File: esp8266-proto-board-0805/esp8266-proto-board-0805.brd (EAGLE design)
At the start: 29.1 x 32.7 mm, 13 parts

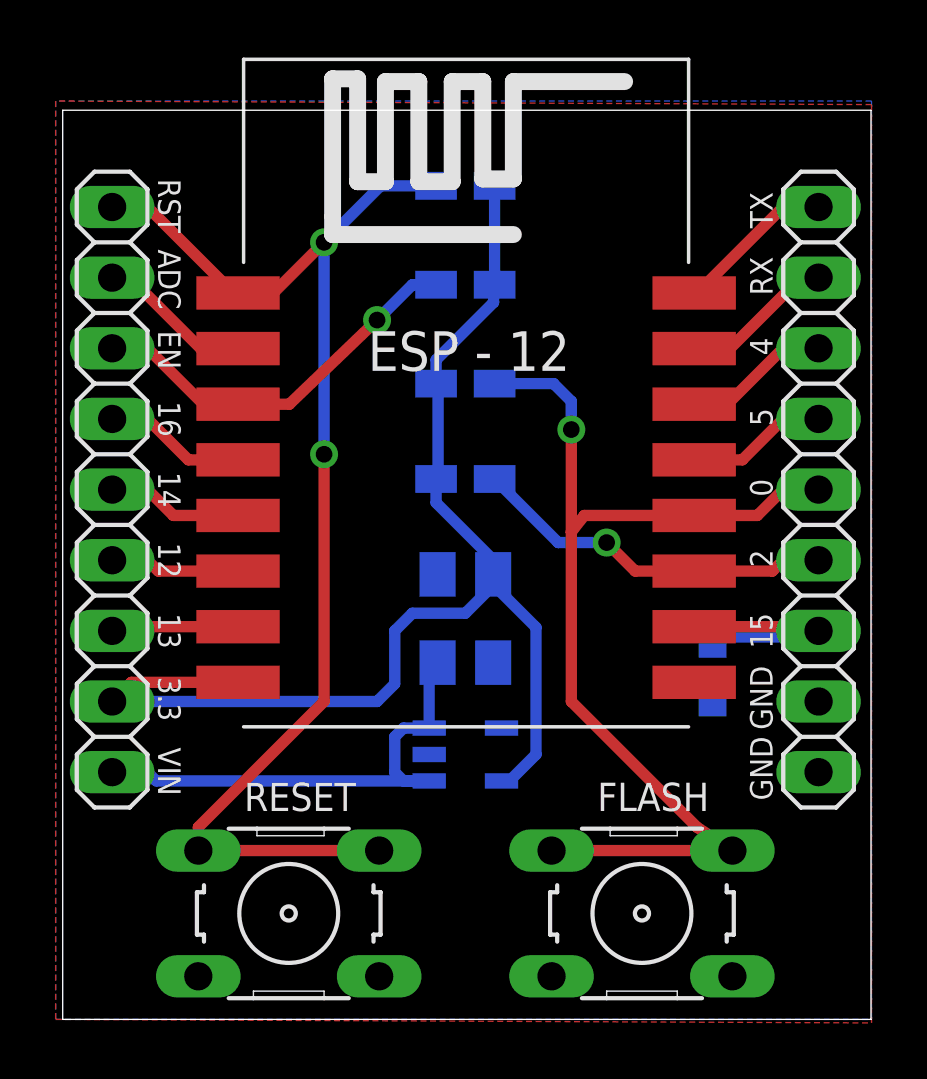
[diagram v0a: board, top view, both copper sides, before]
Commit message: reworked 0805 version with better footprint
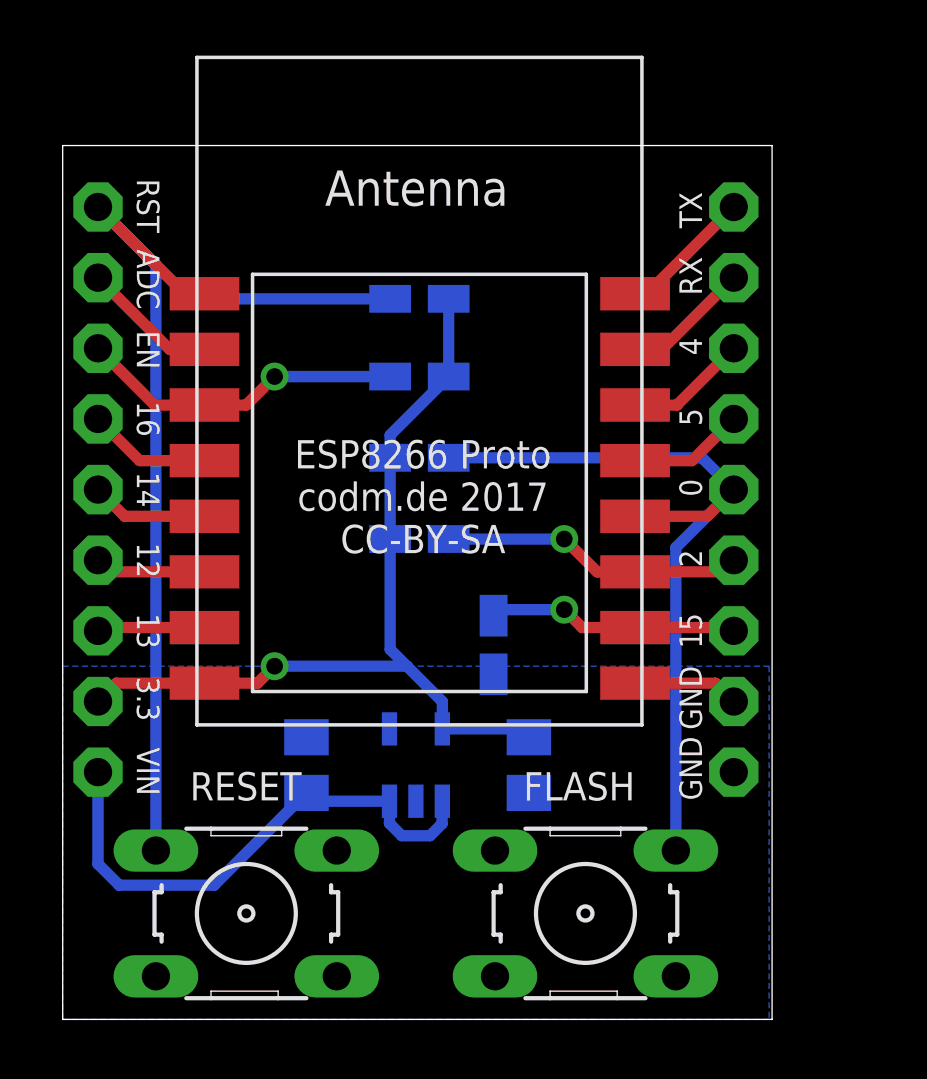
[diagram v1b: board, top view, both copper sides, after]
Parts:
- JP1, JP2: device pinhead:1X09 -> adafruit:1X09-BIG
- U1: device esp8266modules:ESP12-SMD -> adafruit:ESP-12
- moved R5 7.91 mm to (15.5, 13.5)
- moved C2 7.23 mm to (16.8, 9.14), turned to 90 degrees
- moved C1 6.80 mm to (8.76, 9.14), turned to 270 degrees
- moved R1 4.39 mm to (12.8, 25.9)
- moved R2 3.69 mm to (12.8, 23.1)
- moved R3 3.14 mm to (12.8, 20.2)
- moved JP1 3.05 mm to (24.1, 19.1)
- moved R4 2.72 mm to (12.8, 17.3)
- moved U1 2.18 mm to (12.8, 21.6)
- moved S1 2.03 mm to (18.8, 3.81), turned to 0 degrees
- moved VR 1.82 mm to (12.7, 9.14), turned to 0 degrees
- moved S2 1.52 mm to (6.60, 3.81), turned to 0 degrees
- moved JP2 0.51 mm to (1.27, 19.1)
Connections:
- net +3V3: now also U1.8; no longer U1.VCC
- net ADC: now also U1.2; no longer U1.ADC
- net CH_PD: now also U1.3; no longer U1.CH_PD
- net GND: now also S1.4, S2.3, U1.9; no longer S1.1, S1.2, S2.1, S2.2, U1.GND
- net GPIO0: now also S1.2, U1.12; no longer S1.3, S1.4, U1.GPIO0
- net GPIO12: now also U1.6; no longer U1.GPIO12
- net GPIO13: now also U1.7; no longer U1.GPIO13
- net GPIO14: now also U1.5; no longer U1.GPIO14
- net GPIO15: now also U1.10; no longer U1.GPIO15
- net GPIO16: now also U1.4; no longer U1.GPIO16
- net GPIO2: now also U1.11; no longer U1.GPIO2
- net GPIO4: now also U1.14; no longer U1.GPIO4
- net GPIO5: now also U1.13; no longer U1.GPIO5
- net RST: now also S2.1, U1.1; no longer S2.3, S2.4, U1.RESET
- net RX: now also U1.15; no longer U1.RXD0
- net TX: now also U1.16; no longer U1.TXD0
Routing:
- net +3V3: track 47.4 -> 32.0 mm, vias 0 -> 1
- net GPIO0: track 37.8 -> 28.5 mm, vias 1 -> 0
- net GND: track 0.00 -> 3.82 mm
- net CH_PD: track 14.8 -> 11.8 mm
- net GPIO2: track 13.2 -> 10.9 mm
- net RST: track 44.9 -> 43.9 mm, vias 2 -> 0
- net VIN: track 18.5 -> 19.5 mm
- net TX: track 5.75 -> 4.84 mm
- net RX: track 5.53 -> 4.62 mm
- net GPIO5: track 5.08 -> 4.17 mm
- net GPIO4: track 5.31 -> 4.39 mm
- net GPIO13: track 4.59 -> 3.88 mm
- net GPIO16: track 5.14 -> 4.45 mm
- net ADC: track 5.58 -> 4.90 mm
- net GPIO14: track 4.91 -> 4.23 mm
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- removed copper zone on layer 1, net GND
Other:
- board size 29.1 x 32.7 mm -> 25.5 x 31.4 mm
- board text added: "ESP8266 Proto codm.de 2017 CC-BY-SA"

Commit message: moved capacitors
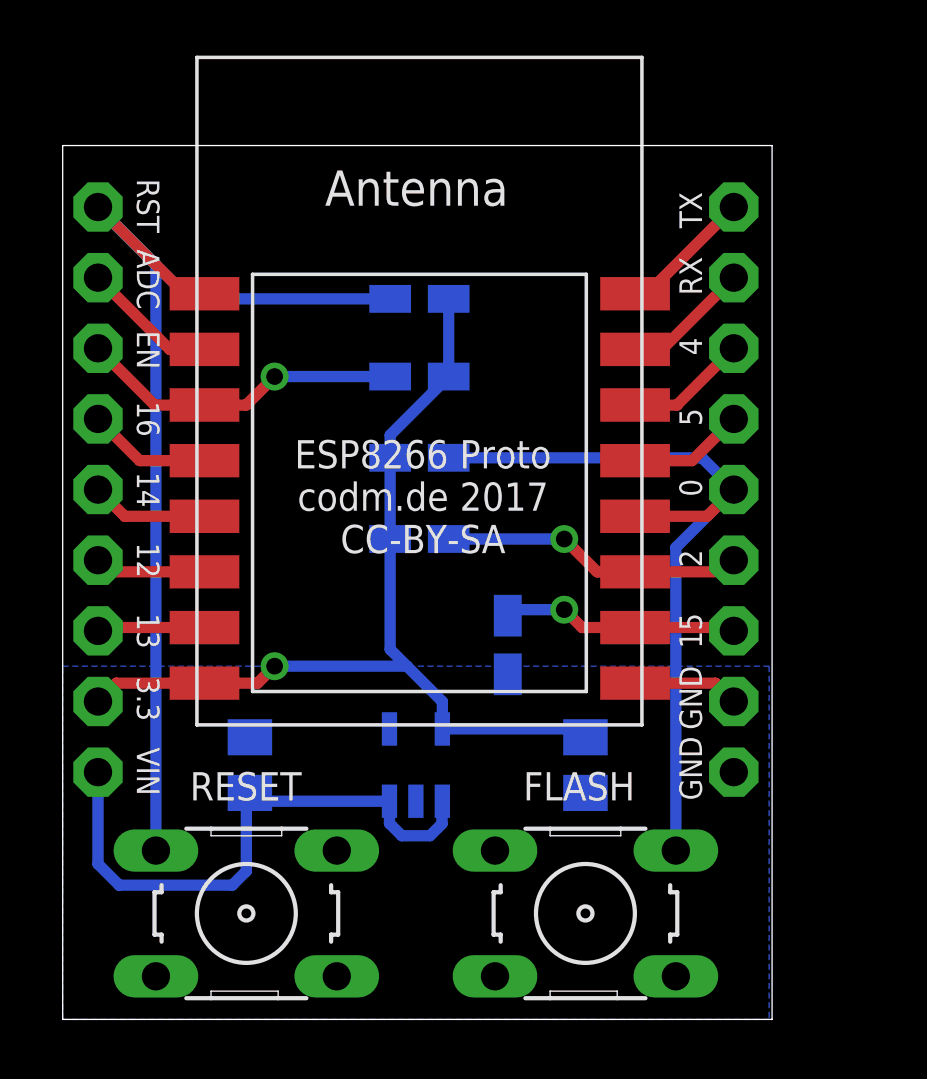
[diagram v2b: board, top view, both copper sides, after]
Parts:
- moved C1 2.03 mm to (6.73, 9.14)
- moved C2 2.03 mm to (18.8, 9.14)
- moved R5 0.51 mm to (16.0, 13.5)
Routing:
- net +3V3: track 32.0 -> 34.0 mm
- net VIN: track 19.5 -> 21.1 mm
- net GPIO15: track 9.09 -> 8.53 mm
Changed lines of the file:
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@@
 </autorouter>
 <elements>
-<element name="C1" library="rcl" package="C0805K" value="1µF" x="8.763" y="9.144" smashed="yes" rot="MR270">
-<attribute name="NAME" x="5.604" y="9.666" size="1.016" layer="26" rot="MR180"/>
-</element>
-<element name="C2" library="rcl" package="C0805K" value="2.2µF" x="16.764" y="9.144" smashed="yes" rot="MR90">
-<attribute name="NAME" x="19.669" y="8.749" size="1.016" layer="26" rot="MR0"/>
+<element name="C1" library="rcl" package="C0805K" value="1µF" x="6.731" y="9.144" smashed="yes" rot="MR270">
+<attribute name="NAME" x="3.572" y="9.666" size="1.016" layer="26" rot="MR180"/>
+</element>
+<element name="C2" library="rcl" package="C0805K" value="2.2µF" x="18.796" y="9.144" smashed="yes" rot="MR90">
+<attribute name="NAME" x="21.701" y="8.749" size="1.016" layer="26" rot="MR0"/>
 </element>
 <element name="JP1" library="adafruit" package="1X09-BIG" value="" x="24.13" y="19.05" smashed="yes" rot="R270">
@@
 <attribute name="NAME" x="8.636" y="17.78" size="1.016" layer="26" rot="MR180"/>
 </element>
-<element name="R5" library="rcl" package="R0805W" value="10kΩ" x="15.494" y="13.462" smashed="yes" rot="MR270">
-<attribute name="NAME" x="16.51" y="13.97" size="1.016" layer="26" rot="MR180"/>
+<element name="R5" library="rcl" package="R0805W" value="10kΩ" x="16.002" y="13.462" smashed="yes" rot="MR270">
+<attribute name="NAME" x="17.018" y="13.97" size="1.016" layer="26" rot="MR180"/>
 </element>
 <element name="S1" library="switch-omron" package="B3F-10XX" value="FLASH" x="18.796" y="3.81" smashed="yes">
@@
 <wire x1="18.676" y1="14.09" x2="18.034" y2="14.732" width="0.4064" layer="1"/>
 <via x="18.034" y="14.732" extent="1-16" drill="0.6" shape="octagon"/>
-<wire x1="18.034" y1="14.732" x2="15.748" y2="14.732" width="0.4064" layer="16"/>
-<wire x1="15.748" y1="14.732" x2="15.5305" y2="14.5145" width="0.4064" layer="16"/>
-<wire x1="15.5305" y1="14.5145" x2="15.5305" y2="14.478" width="0.4064" layer="16"/>
-<wire x1="15.5305" y1="14.478" x2="15.494" y2="14.5145" width="0.4064" layer="16"/>
+<wire x1="18.034" y1="14.732" x2="16.2195" y2="14.732" width="0.4064" layer="16"/>
+<wire x1="16.2195" y1="14.732" x2="16.002" y2="14.5145" width="0.4064" layer="16"/>
 </signal>
 <signal name="GND">
@@
 <contactref element="R3" pad="1"/>
 <contactref element="R4" pad="1"/>
-<wire x1="13.65" y1="10.4441" x2="16.4639" y2="10.4441" width="0.4064" layer="16"/>
-<wire x1="16.4639" y1="10.4441" x2="16.764" y2="10.144" width="0.4064" layer="16"/>
 <wire x1="13.65" y1="10.4441" x2="13.65" y2="11.43" width="0.4064" layer="16"/>
 <wire x1="11.7745" y1="17.272" x2="11.7745" y2="20.193" width="0.4064" layer="16"/>
@@
 <wire x1="1.93" y1="12.09" x2="1.27" y2="11.43" width="0.4064" layer="1"/>
 <wire x1="11.7745" y1="13.3055" x2="12.38" y2="12.7" width="0.4064" layer="16"/>
-<wire x1="12.413" y1="12.667" x2="13.65" y2="11.43" width="0.4064" layer="16"/>
+<wire x1="12.38" y1="12.7" x2="13.65" y2="11.43" width="0.4064" layer="16"/>
 <wire x1="11.7745" y1="17.272" x2="11.7745" y2="13.3055" width="0.4064" layer="16"/>
 <wire x1="5.0984" y1="12.09" x2="7.01" y2="12.09" width="0.4064" layer="1"/>
@@
 <via x="7.62" y="12.7" extent="1-16" drill="0.6" shape="octagon"/>
 <wire x1="7.62" y1="12.7" x2="12.38" y2="12.7" width="0.4064" layer="16"/>
-<wire x1="12.38" y1="12.7" x2="12.413" y2="12.667" width="0.4064" layer="16"/>
+<wire x1="13.65" y1="10.4441" x2="18.4959" y2="10.4441" width="0.4064" layer="16"/>
+<wire x1="18.4959" y1="10.4441" x2="18.796" y2="10.144" width="0.4064" layer="16"/>
 </signal>
 <signal name="VIN">
@@
 <contactref element="C1" pad="2"/>
 <contactref element="VR" pad="3"/>
-<wire x1="11.75" y1="7.8439" x2="9.0631" y2="7.8439" width="0.4064" layer="16"/>
-<wire x1="9.0631" y1="7.8439" x2="8.763" y2="8.144" width="0.4064" layer="16"/>
-<wire x1="1.27" y1="8.89" x2="1.27" y2="5.588" width="0.4064" layer="16"/>
-<wire x1="1.27" y1="5.588" x2="2.032" y2="4.826" width="0.4064" layer="16"/>
-<wire x1="2.032" y1="4.826" x2="5.445" y2="4.826" width="0.4064" layer="16"/>
-<wire x1="5.445" y1="4.826" x2="8.763" y2="8.144" width="0.4064" layer="16"/>
 <wire x1="11.75" y1="7.8439" x2="11.75" y2="7.046" width="0.4064" layer="16"/>
 <wire x1="11.75" y1="7.046" x2="12.192" y2="6.604" width="0.4064" layer="16"/>
@@
 <wire x1="13.6398" y1="7.0358" x2="13.6398" y2="7.8337" width="0.4064" layer="16"/>
 <wire x1="13.6398" y1="7.8337" x2="13.65" y2="7.8439" width="0.4064" layer="16"/>
+<wire x1="1.27" y1="8.89" x2="1.27" y2="5.588" width="0.4064" layer="16"/>
+<wire x1="1.27" y1="5.588" x2="2.032" y2="4.826" width="0.4064" layer="16"/>
+<wire x1="2.032" y1="4.826" x2="6.096" y2="4.826" width="0.4064" layer="16"/>
+<wire x1="6.096" y1="4.826" x2="6.604" y2="5.334" width="0.4064" layer="16"/>
+<wire x1="6.604" y1="5.334" x2="6.604" y2="7.62" width="0.4064" layer="16"/>
+<wire x1="6.604" y1="7.62" x2="6.604" y2="8.017" width="0.4064" layer="16"/>
+<wire x1="6.604" y1="8.017" x2="6.731" y2="8.144" width="0.4064" layer="16"/>
+<wire x1="11.75" y1="7.8439" x2="6.8279" y2="7.8439" width="0.4064" layer="16"/>
+<wire x1="6.8279" y1="7.8439" x2="6.604" y2="7.62" width="0.4064" layer="16"/>
 </signal>
 <signal name="RX">

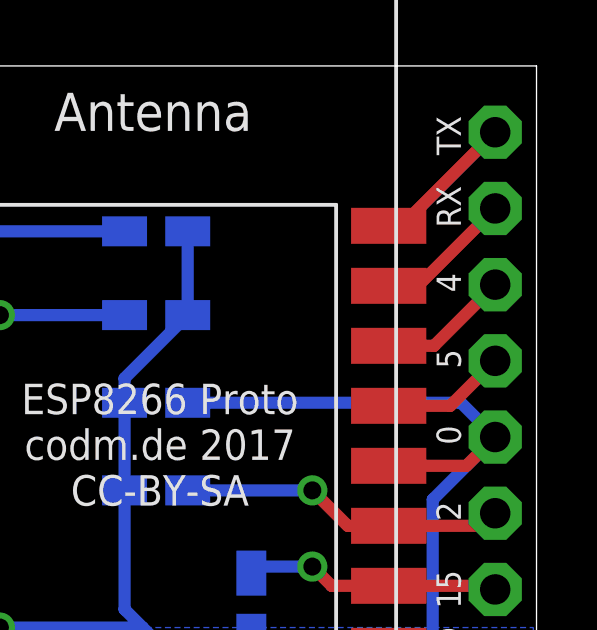
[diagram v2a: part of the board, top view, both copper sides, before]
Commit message: fixed mixed up gpio5/gpio4 in esp-lib part
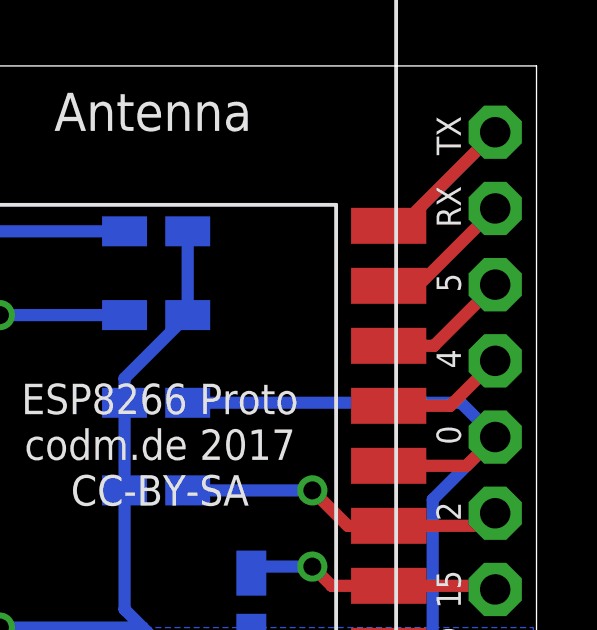
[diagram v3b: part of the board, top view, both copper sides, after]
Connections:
- net GPIO4: now also JP1.4, U1.13; no longer JP1.3, U1.14
- net GPIO5: now also JP1.3, U1.14; no longer JP1.4, U1.13
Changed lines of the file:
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@@
 <text x="22.987" y="28.448" size="0.8128" layer="25" rot="R90">TX</text>
 <text x="22.987" y="26.035" size="0.8128" layer="25" rot="R90">RX</text>
-<text x="22.987" y="23.876" size="0.8128" layer="25" rot="R90">4</text>
-<text x="22.987" y="21.336" size="0.8128" layer="25" rot="R90">5</text>
+<text x="22.987" y="21.336" size="0.8128" layer="25" rot="R90">4</text>
+<text x="22.987" y="23.876" size="0.8128" layer="25" rot="R90">5</text>
 <text x="22.987" y="18.796" size="0.8128" layer="25" rot="R90">0</text>
 <text x="22.987" y="16.256" size="0.8128" layer="25" rot="R90">2</text>
@@
 <wire x1="1.39" y1="14.09" x2="1.27" y2="13.97" width="0.4064" layer="1"/>
 </signal>
-<signal name="GPIO4">
+<signal name="GPIO5">
 <contactref element="U1" pad="14"/>
 <contactref element="JP1" pad="3"/>
@@
 <wire x1="22.09" y1="22.09" x2="24.13" y2="24.13" width="0.4064" layer="1"/>
 </signal>
-<signal name="GPIO5">
+<signal name="GPIO4">
 <contactref element="U1" pad="13"/>
 <contactref element="JP1" pad="4"/>
